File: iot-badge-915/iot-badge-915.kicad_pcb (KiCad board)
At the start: 2 copper layers, 70 x 100 mm, 64 parts, among them J1 USB_C_Receptacle_USB2.0, J2 Wire ANT, Q1 BC847, Q2 BC847, Q3 BC847, SW1 SW_Push, SW2 SW_Push, SW3 SW_Push, SW4 SW_Push, SW5 SW_Push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

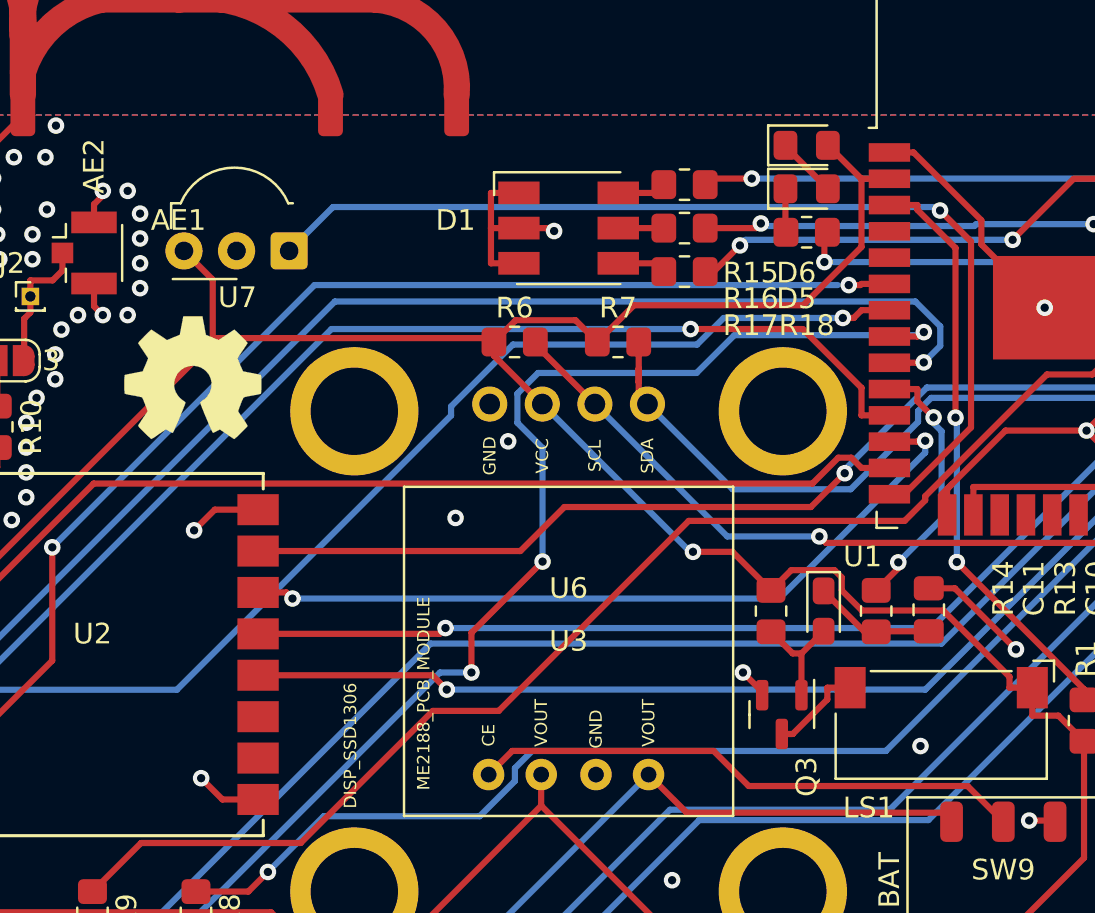
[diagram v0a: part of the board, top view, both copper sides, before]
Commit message: changed ir leds polarity, PSU silk and bypass jumper
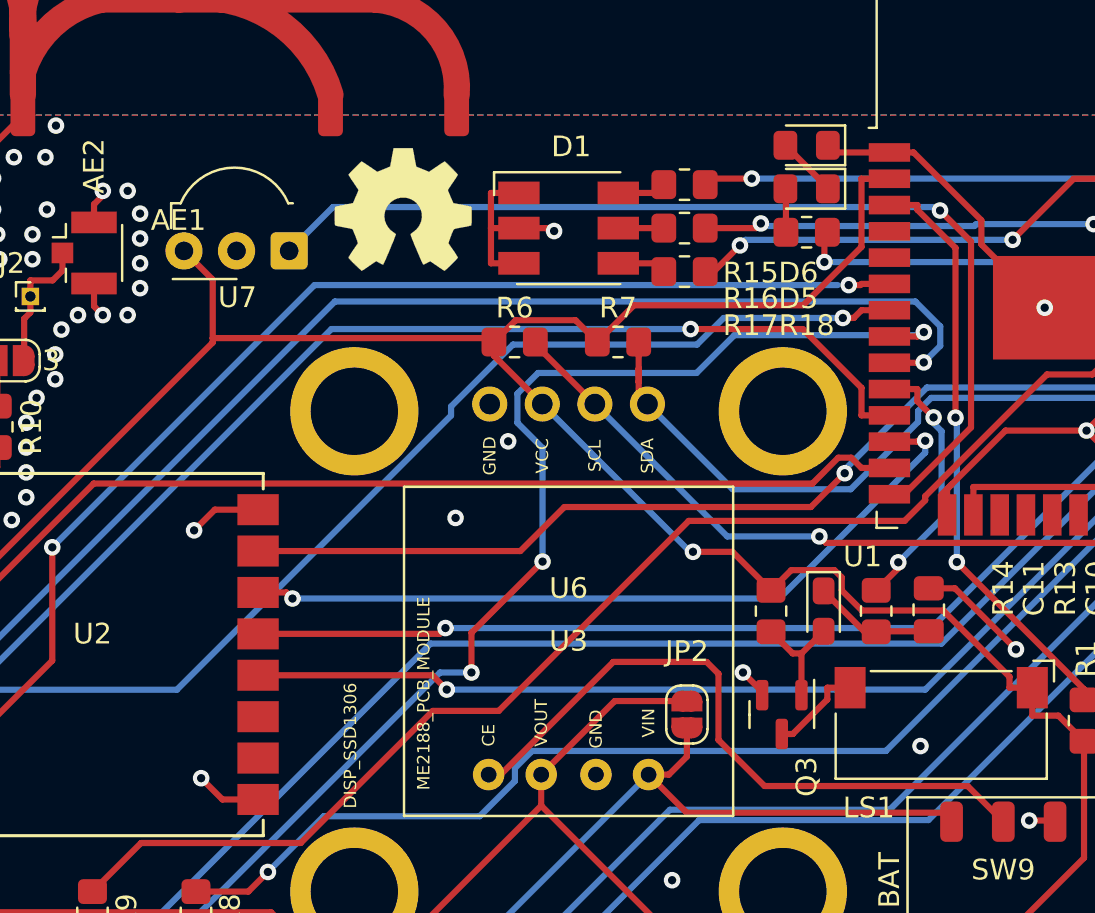
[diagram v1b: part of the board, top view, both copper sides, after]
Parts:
- added JP2: SolderJumper_2_Open, Jumper:SolderJumper-2_P1.3mm_Open_RoundedPad1.0x1.5mm, F.Cu at (140.7, 95.0)
- moved SYMB2 13.0 mm to (127.0, 70.6)
- turned D5 to 180 degrees
- turned D6 to 180 degrees
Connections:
- D6 pad 1: Net-(D5-Pad2) -> Earth
- D6 pad 2: +3V3 -> Net-(D5-Pad1)
- R18 pad 1: Net-(D5-Pad1) -> Net-(D5-Pad2)
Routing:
- net Net-(R11-Pad2): track 58.8 -> 67.3 mm
- net Net-(SW9-Pad5): track 26.8 -> 32.2 mm
- net +BATT: track 53.9 -> 57.5 mm
- net Earth: track 199.7 -> 202.8 mm
- net +3V3: track 115.2 -> 113.0 mm
- net Net-(D5-Pad1): track 2.11 -> 3.00 mm
- net Net-(D5-Pad2): track 2.95 -> 2.15 mm
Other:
- board text added: "VIN"

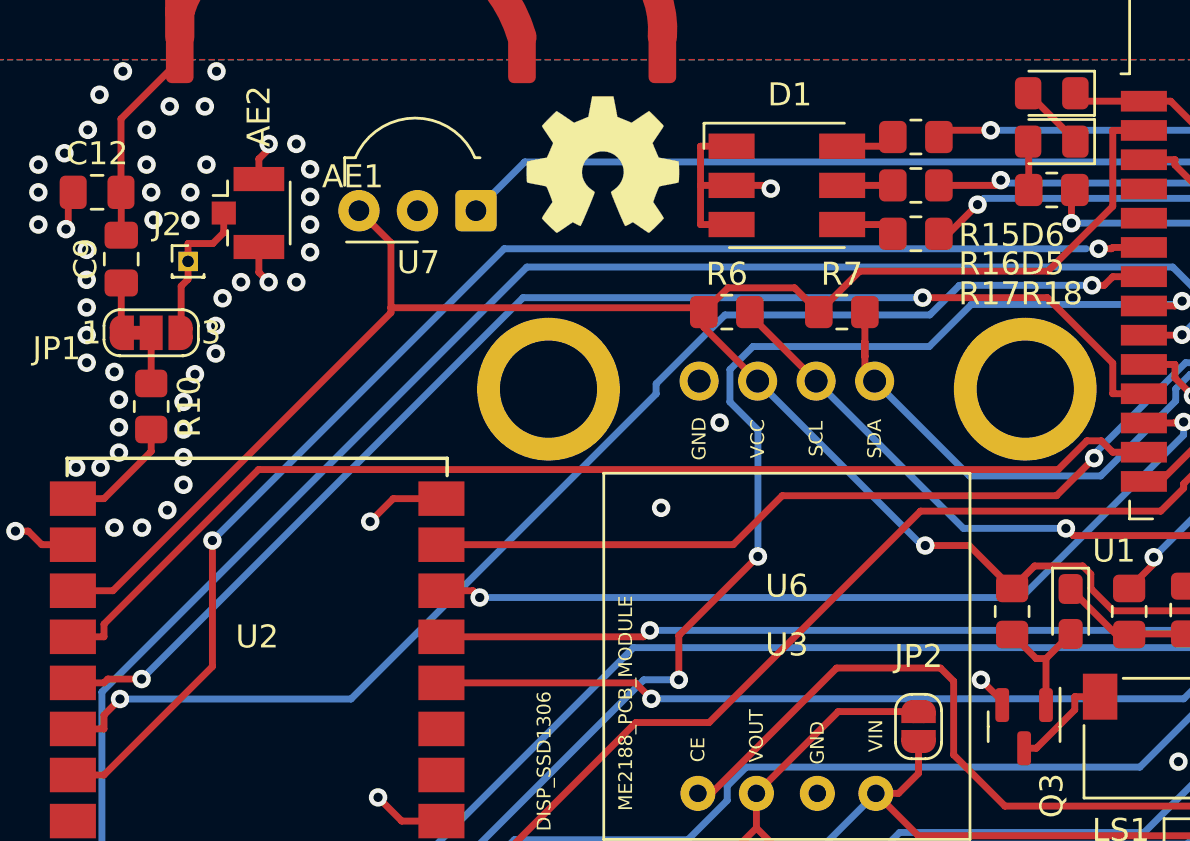
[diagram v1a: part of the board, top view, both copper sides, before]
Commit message: added external i2c pins
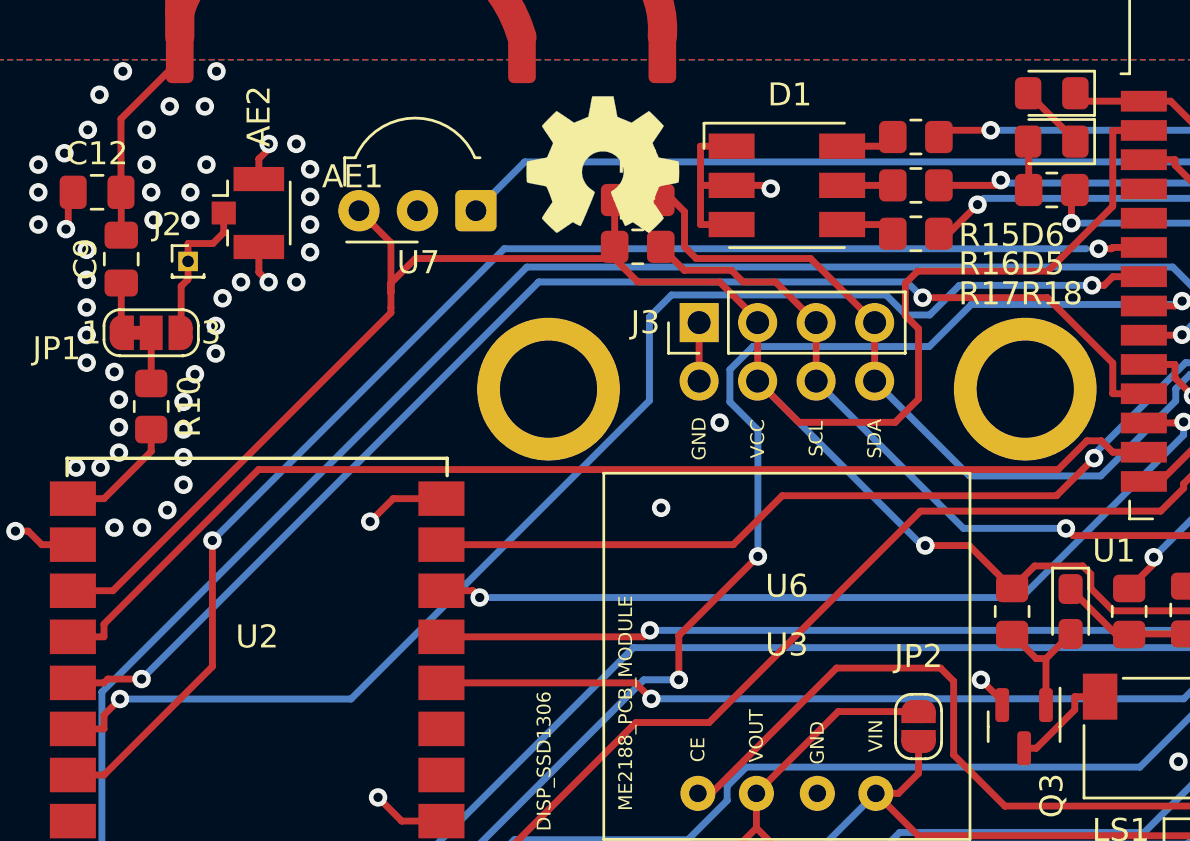
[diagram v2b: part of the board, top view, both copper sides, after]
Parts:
- added J3: Conn_01x04_Male, Connector_PinHeader_2.54mm:PinHeader_1x04_P2.54mm_Vertical, F.Cu at (131.2, 77.5)
- moved R7 10.1 mm to (128.5, 72.1)
- moved R6 4.79 mm to (128.5, 74.2)
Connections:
- net Net-(R6-Pad2) renamed /SCL
- net Net-(R7-Pad2) renamed /SDA
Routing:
- net /SDA: track 39.4 -> 50.5 mm
- net +3V3: track 113.0 -> 121.9 mm
- net /SCL: track 35.6 -> 42.0 mm
- net Net-(U1-Pad7): track 55.2 -> 57.8 mm
- net Earth: track 202.8 -> 205.3 mm
- net Net-(U1-Pad11): track 55.9 -> 56.5 mm

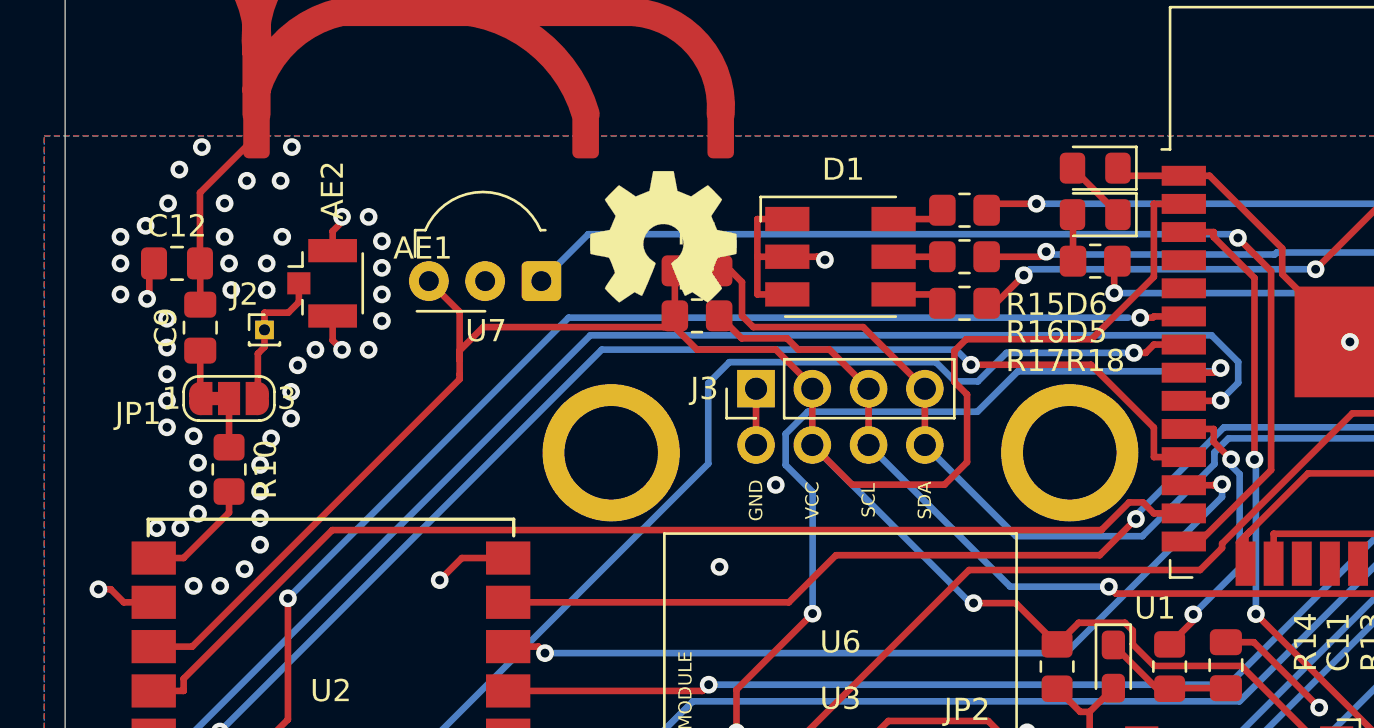
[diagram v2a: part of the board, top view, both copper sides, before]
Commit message: shifted ant match elements to the left
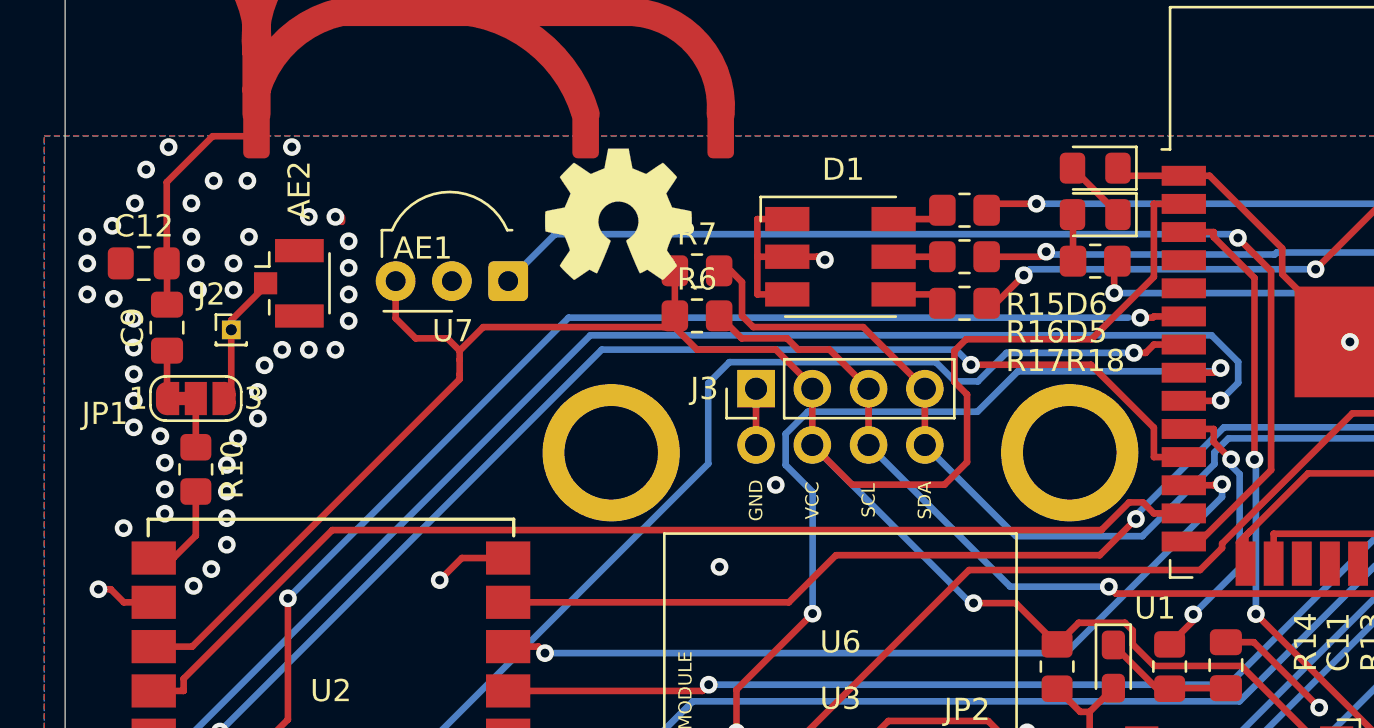
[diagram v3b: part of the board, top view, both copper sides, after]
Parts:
- moved SYMB2 2.27 mm to (125.0, 69.6)
- moved AE2 1.50 mm to (110.1, 72.7)
- moved C12 1.50 mm to (103.5, 71.8)
- moved C9 1.50 mm to (104.6, 74.7)
- moved J2 1.50 mm to (107.5, 74.8)
- moved JP1 1.50 mm to (105.9, 77.9)
- moved R10 1.50 mm to (105.9, 81.1)
- moved U7 1.50 mm to (120.0, 72.6)
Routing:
- net Earth: track 205.3 -> 200.6 mm, vias 104 -> 102
- net Net-(AE1-Pad1): track 8.56 -> 10.4 mm
- net /IRDEC-12: track 48.8 -> 50.3 mm
- net +3V3: track 121.9 -> 122.9 mm
- net Net-(R10-Pad2): track 5.20 -> 4.31 mm
- net Net-(AE2-Pad1): track 6.60 -> 5.97 mm

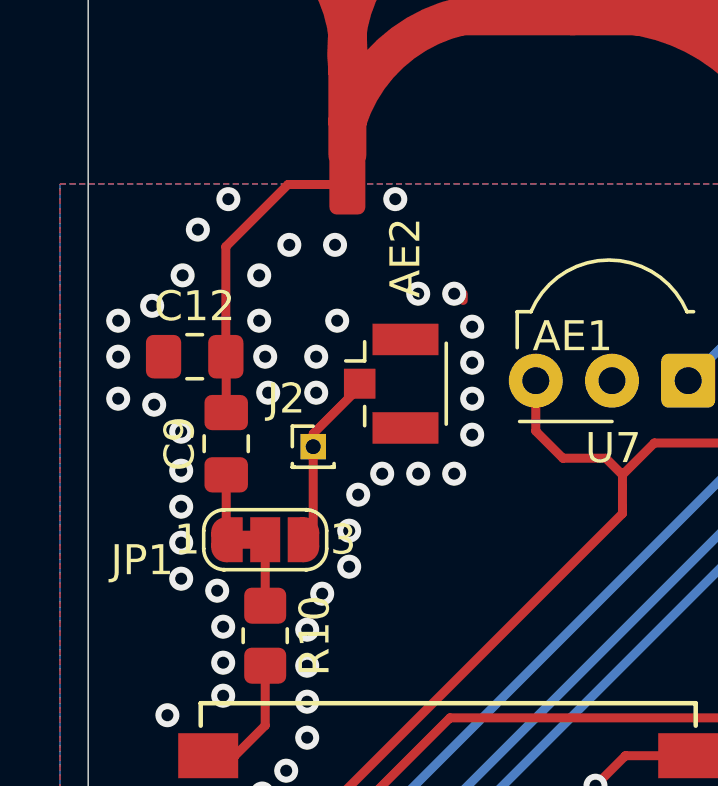
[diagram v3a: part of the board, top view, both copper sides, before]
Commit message: added tuning cap an inductor to ant circuit
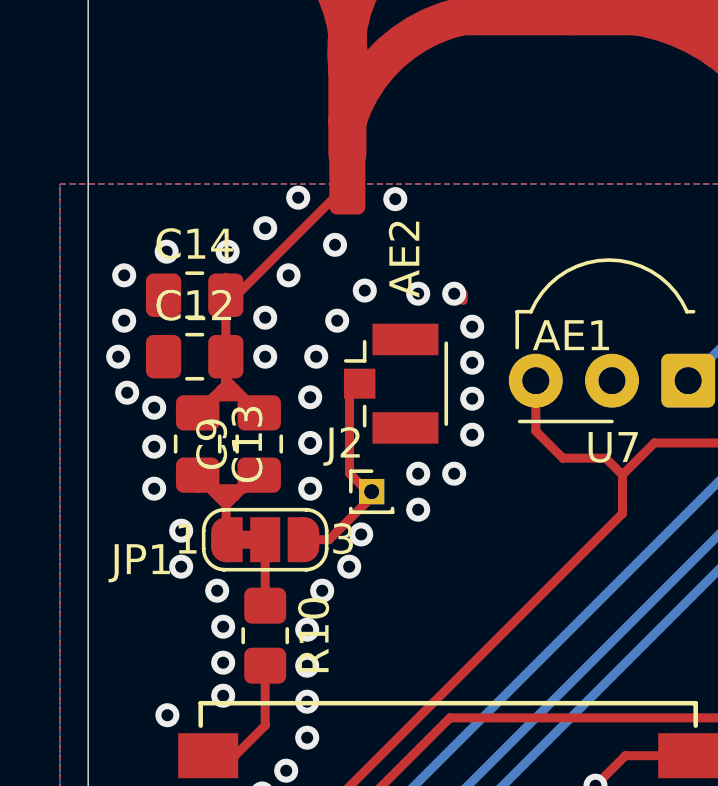
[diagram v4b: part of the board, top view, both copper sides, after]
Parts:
- added C13: C, Capacitor_SMD:C_0805_2012Metric_Pad1.18x1.45mm_HandSolder, F.Cu at (103.7, 74.7)
- added C14: C, Capacitor_SMD:C_0805_2012Metric_Pad1.18x1.45mm_HandSolder, F.Cu at (103.5, 69.8)
- moved J2 2.46 mm to (109.5, 76.3)
- moved C9 1.10 mm to (105.7, 74.7)
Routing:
- net Net-(AE1-Pad1): track 10.4 -> 18.1 mm
- net Net-(C9-Pad2): track 2.16 -> 7.56 mm
- net Net-(AE2-Pad1): track 5.97 -> 7.25 mm

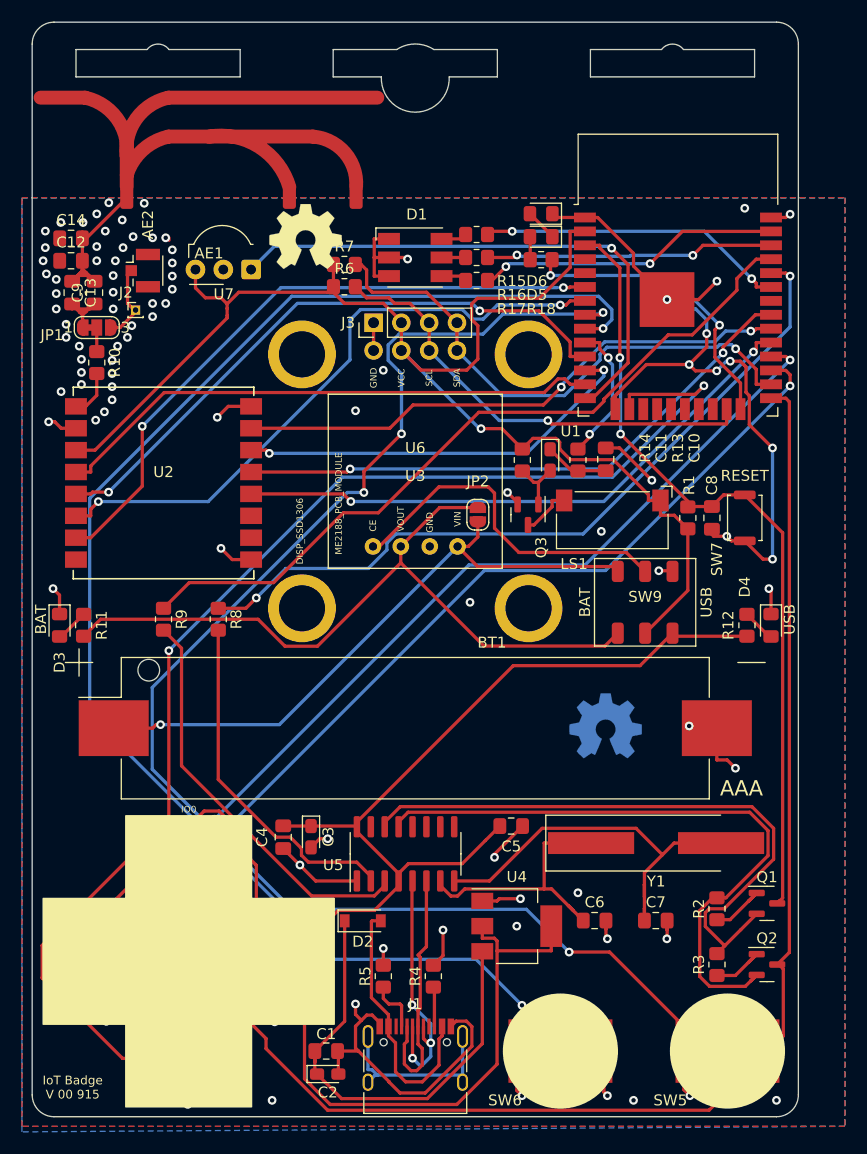
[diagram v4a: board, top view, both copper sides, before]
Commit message: enlarged AAA bat footprint pads
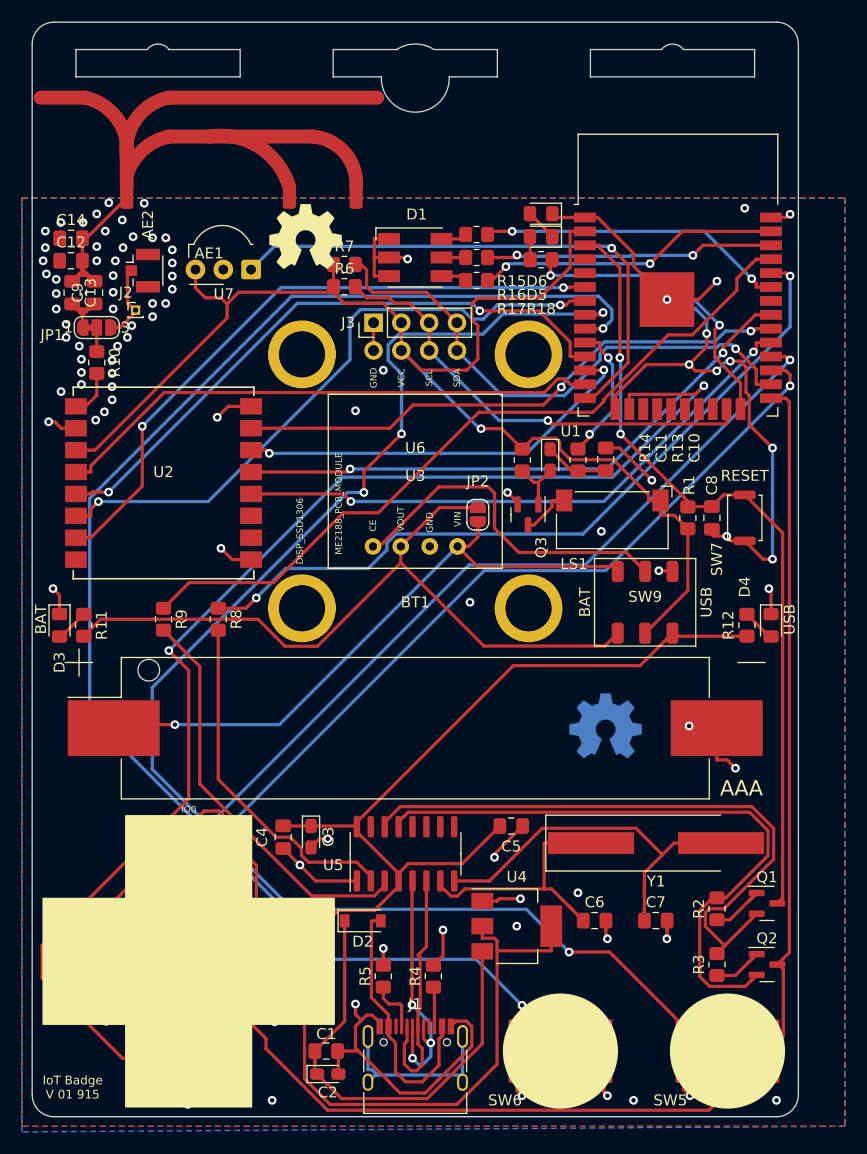
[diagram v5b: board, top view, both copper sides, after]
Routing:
- net /SW2-13: track 123.0 -> 124.5 mm
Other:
- board text added: "IoT Badge V 01 915"
- board text removed: "IoT Badge V 00 915"
